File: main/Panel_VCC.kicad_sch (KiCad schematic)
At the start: 8 parts

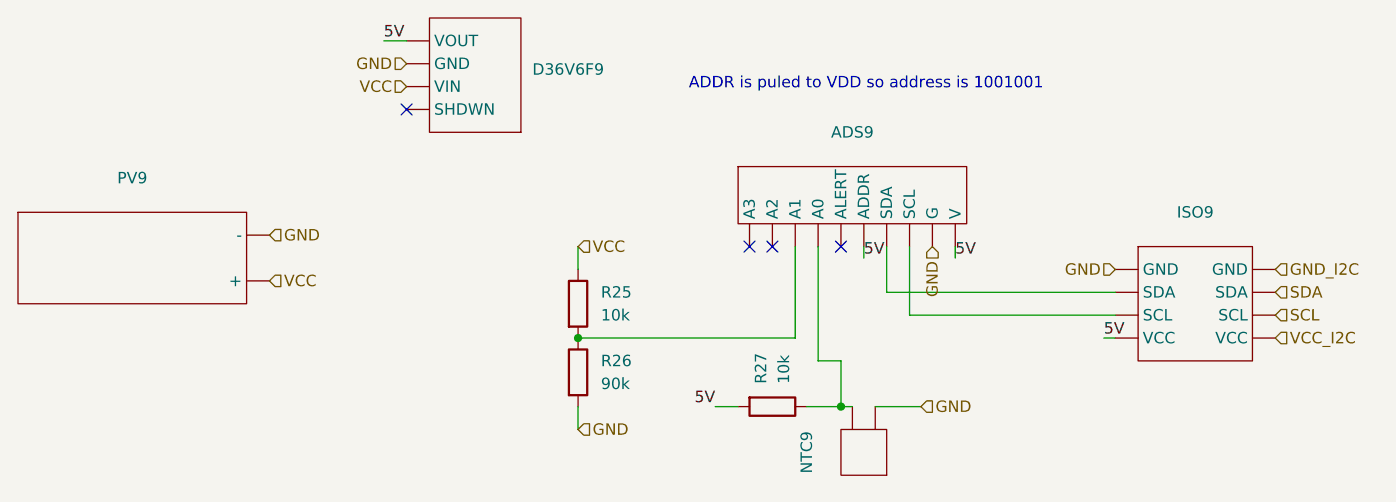
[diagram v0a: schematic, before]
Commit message: Added Central Control Unit Added Jetson Orin Nano
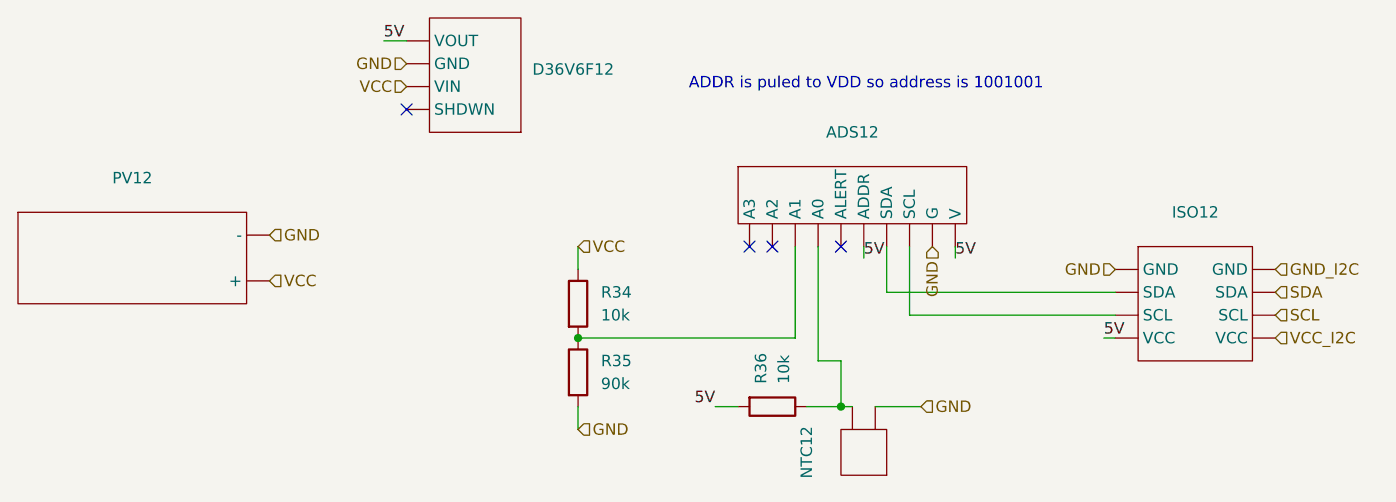
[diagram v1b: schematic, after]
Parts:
- renumbered ADS9 to ADS12, D36V6F9 to D36V6F12, ISO9 to ISO12, NTC9 to NTC12, PV9 to PV12, R25 to R34, R26 to R35, R27 to R36
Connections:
- new net: ADS12. (V), ISO12. (VCC) (x2)
- new net: ADS12. (V), NTC12., R36.1
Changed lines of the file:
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@@
 		(dnp no)
 		(fields_autoplaced yes)
-		(property "Reference" "PV9"
+		(property "Reference" "PV12"
 			(at 52.07 67.31 0)
 			(effects
@@
 		(dnp no)
 		(fields_autoplaced yes)
-		(property "Reference" "ISO9"
+		(property "Reference" "ISO12"
 			(at 170.18 71.12 0)
 			(effects
@@
 		(dnp no)
 		(fields_autoplaced yes)
-		(property "Reference" "NTC9"
+		(property "Reference" "NTC12"
 			(at 127 97.79 90)
 			(effects
@@
 		(dnp no)
 		(fields_autoplaced yes)
-		(property "Reference" "ADS9"
+		(property "Reference" "ADS12"
 			(at 132.08 62.23 0)
 			(effects
@@
 		(dnp no)
 		(fields_autoplaced yes)
-		(property "Reference" "R26"
+		(property "Reference" "R35"
 			(at 104.14 87.6299 0)
 			(effects
@@
 		(dnp no)
 		(fields_autoplaced yes)
-		(property "Reference" "R27"
+		(property "Reference" "R36"
 			(at 121.9199 90.17 0)
 			(effects
@@
 		(dnp no)
 		(fields_autoplaced yes)
-		(property "Reference" "R25"
+		(property "Reference" "R34"
 			(at 104.14 80.0099 0)
 			(effects
@@
 		(dnp no)
 		(fields_autoplaced yes)
-		(property "Reference" "D36V6F9"
+		(property "Reference" "D36V6F12"
 			(at 96.52 55.2449 0)
 			(effects

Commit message: added logos, oranised sheets, final version
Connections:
- new net: ADS12. (V), ISO12. (VCC) (x2)
- new net: ADS12. (V), NTC12., R36.1
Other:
- company: (none) -> Designers: Krzysztof Grajek, Wojtek Kołodziej

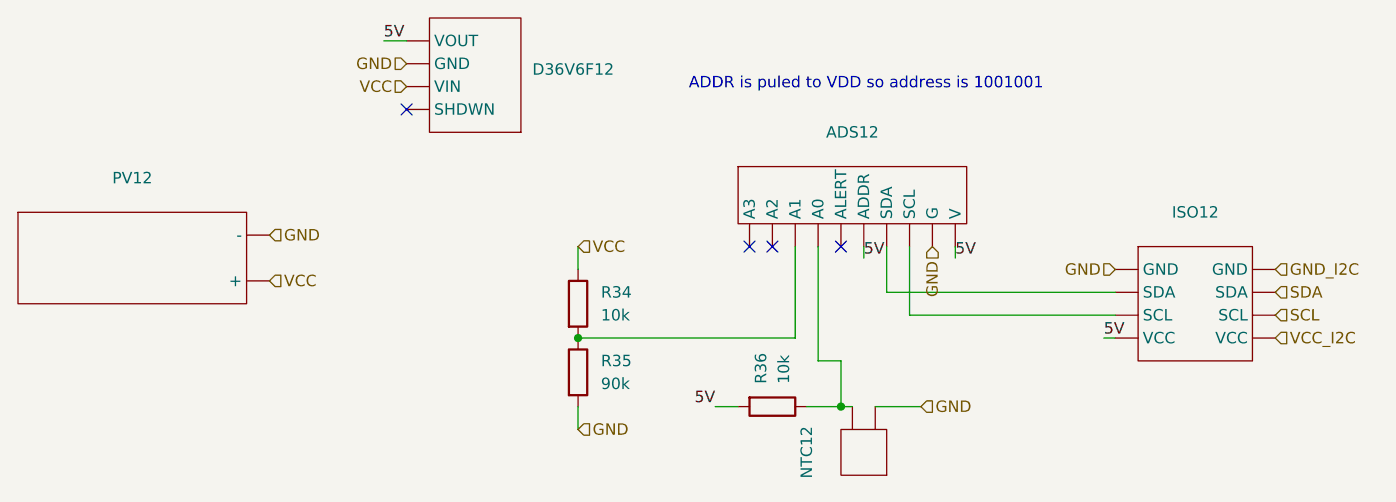
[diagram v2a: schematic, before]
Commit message: Changed name of Adafruit 4903(i2c spearator). Changed values of resistors used in panels
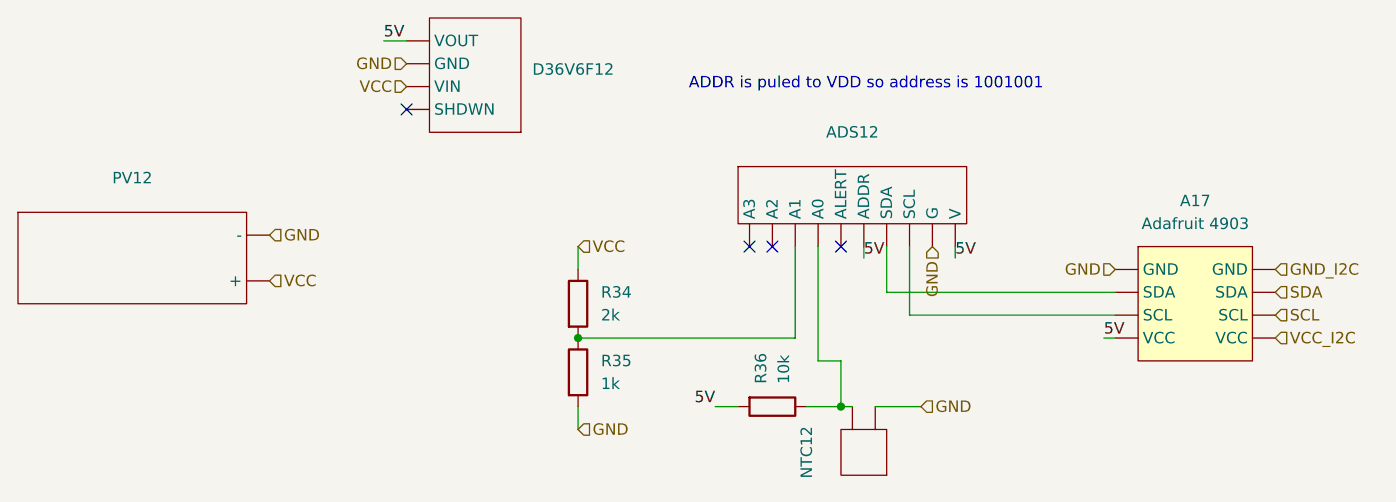
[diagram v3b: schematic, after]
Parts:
- removed ISO12: ~, symbol New_Library_0:Bidirectional I2C Isolator
- added A17: Adafruit 4903, symbol New_Library_0:Adafruit_4903
- R34: value 10k -> 2k
- R35: value 90k -> 1k
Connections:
- net 5V: now also A17. (VCC)
- net GND: now also A17. (VCC)
- net GND_I2C: now also A17. (VCC)
- net SCL: now also A17. (VCC)
- net SDA: now also A17. (VCC)
- net VCC_I2C: now also A17. (VCC)
- new net: A17. (VCC), ADS12. (V) (x2)
- new net: ADS12. (V), NTC12., R36.1
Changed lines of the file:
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@@
 	)
 	(symbol
-		(lib_id "New_Library_0:Bidirectional I2C Isolator")
+		(lib_id "New_Library_0:Adafruit_4903")
 		(at 170.18 81.28 0)
 		(unit 1)
@@
 		(dnp no)
 		(fields_autoplaced yes)
-		(property "Reference" "ISO12"
-			(at 170.18 71.12 0)
-			(effects
-				(font
-					(size 1.27 1.27)
-				)
-			)
-		)
-		(property "Value" "~"
-			(at 170.18 73.66 0)
+		(property "Reference" "A17"
+			(at 170.18 69.85 0)
+			(effects
+				(font
+					(size 1.27 1.27)
+				)
+			)
+		)
+		(property "Value" "Adafruit 4903"
+			(at 170.18 72.39 0)
 			(effects
 				(font
@@
 			(project "main"
 				(path "/54fbbba9-a737-4199-9a4b-f9fa49b3de5e/42b38d5d-5c36-4712-95e4-9fdfab477064/6cfcbdb0-aed9-4bf5-b5b7-5d12e64435b6"
-					(reference "ISO12")
+					(reference "A17")
 					(unit 1)
 				)
 				(path "/54fbbba9-a737-4199-9a4b-f9fa49b3de5e/42b38d5d-5c36-4712-95e4-9fdfab477064/6faa4d2a-3148-4c79-9699-af4299296d27"
-					(reference "ISO9")
+					(reference "A14")
 					(unit 1)
 				)
 				(path "/54fbbba9-a737-4199-9a4b-f9fa49b3de5e/42b38d5d-5c36-4712-95e4-9fdfab477064/85a69679-bf7c-4613-951c-5fe9591916d9"
-					(reference "ISO13")
+					(reference "A18")
 					(unit 1)
 				)
 				(path "/54fbbba9-a737-4199-9a4b-f9fa49b3de5e/42b38d5d-5c36-4712-95e4-9fdfab477064/9fddd8d5-34c0-4e07-a46e-1d9a346c3d97"
-					(reference "ISO11")
+					(reference "A16")
 					(unit 1)
 				)
 				(path "/54fbbba9-a737-4199-9a4b-f9fa49b3de5e/42b38d5d-5c36-4712-95e4-9fdfab477064/a35a0fc2-c5b3-42f6-81f7-38421381f330"
-					(reference "ISO10")
+					(reference "A15")
 					(unit 1)
 				)
 				(path "/54fbbba9-a737-4199-9a4b-f9fa49b3de5e/42b38d5d-5c36-4712-95e4-9fdfab477064/ae956b07-f0d0-4016-86a0-bf6fc2aeb97f"
-					(reference "ISO16")
+					(reference "A21")
 					(unit 1)
 				)
 				(path "/54fbbba9-a737-4199-9a4b-f9fa49b3de5e/42b38d5d-5c36-4712-95e4-9fdfab477064/ec3047b9-e591-40d3-8660-9274d804d577"
-					(reference "ISO14")
+					(reference "A19")
 					(unit 1)
 				)
 				(path "/54fbbba9-a737-4199-9a4b-f9fa49b3de5e/42b38d5d-5c36-4712-95e4-9fdfab477064/f723695a-1365-4026-81d9-82c620c5e3e6"
-					(reference "ISO15")
+					(reference "A20")
 					(unit 1)
 				)
@@
 			)
 		)
-		(property "Value" "90k"
+		(property "Value" "1k"
 			(at 104.14 90.1699 0)
 			(effects
@@
 			)
 		)
-		(property "Value" "10k"
+		(property "Value" "2k"
 			(at 104.14 82.5499 0)
 			(effects
